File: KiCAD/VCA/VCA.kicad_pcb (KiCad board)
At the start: 4 copper layers, 30 x 100 mm, 17 parts, among them J1 VIN, J2 VC, J3 VOUT, J4 Conn_01x03_Pin, Q1 J172, Q2 J172, U1 LT1006

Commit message: Make VCA 2-Layer
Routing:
- net VSS: track 0.00 -> 62.0 mm
- net VDD: track 0.00 -> 2.69 mm
- net Net-(Q2-D): track 33.1 -> 31.8 mm
- added copper zone on B.Cu, net VDD
- removed copper zone on B.Cu, net GND
- removed copper zone on In1.Cu, net VDD
- removed copper zone on In2.Cu, net VSS
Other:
- copper layers 4 -> 2
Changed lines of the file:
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@@
 	(layers
 		(0 "F.Cu" signal)
-		(4 "In1.Cu" signal)
-		(6 "In2.Cu" signal)
 		(2 "B.Cu" signal)
 		(9 "F.Adhes" user "F.Adhesive")
@@
 			)
 			(layer "dielectric 1"
-				(type "prepreg")
-				(thickness 0.1)
-				(material "FR4")
-				(epsilon_r 4.5)
-				(loss_tangent 0.02)
-			)
-			(layer "In1.Cu"
-				(type "copper")
-				(thickness 0.035)
-			)
-			(layer "dielectric 2"
 				(type "core")
-				(thickness 1.24)
-				(material "FR4")
-				(epsilon_r 4.5)
-				(loss_tangent 0.02)
-			)
-			(layer "In2.Cu"
-				(type "copper")
-				(thickness 0.035)
-			)
-			(layer "dielectric 3"
-				(type "prepreg")
-				(thickness 0.1)
+				(thickness 1.51)
 				(material "FR4")
 				(epsilon_r 4.5)
@@
 			(net 0)
 			(net_name "")
-			(layers "F.Cu" "In1.Cu" "In2.Cu")
+			(layer "F.Cu")
 			(hatch full 0.508)
 			(connect_pads
@@
 			(net 0)
 			(net_name "")
-			(layers "F.Cu" "In1.Cu" "In2.Cu")
+			(layer "F.Cu")
 			(hatch full 0.508)
 			(connect_pads
@@
 			(net 0)
 			(net_name "")
-			(layers "F.Cu" "In1.Cu" "In2.Cu")
+			(layer "F.Cu")
 			(hatch full 0.508)
 			(connect_pads
@@
 	)
 	(segment
+		(start 124.5 100.115001)
+		(end 124.5 92.000001)
+		(width 0.5)
+		(layer "F.Cu")
+		(net 1)
+	)
+	(segment
+		(start 124.5 92.000001)
+		(end 127.5 89.000001)
+		(width 0.5)
+		(layer "F.Cu")
+		(net 1)
+	)
+	(segment
+		(start 126.195 101.810001)
+		(end 124.5 100.115001)
+		(width 0.5)
+		(layer "F.Cu")
+		(net 1)
+	)
+	(segment
+		(start 130 105.615001)
+		(end 130 111.385404)
+		(width 0.5)
+		(layer "B.Cu")
+		(net 1)
+	)
+	(segment
+		(start 139.5 120.885404)
+		(end 139.5 143.55)
+		(width 0.5)
+		(layer "B.Cu")
+		(net 1)
+	)
+	(segment
+		(start 130 111.385404)
+		(end 139.5 120.885404)
+		(width 0.5)
+		(layer "B.Cu")
+		(net 1)
+	)
+	(segment
+		(start 126.195 101.810001)
+		(end 130 105.615001)
+		(width 0.5)
+		(layer "B.Cu")
+		(net 1)
+	)
+	(segment
+		(start 137.5 136.6)
+		(end 139.4 134.7)
+		(width 0.5)
+		(layer "F.Cu")
+		(net 2)
+	)
+	(segment
 		(start 125.04 62.62)
 		(end 125.04 77.43)
@@
 		(end 136.999999 110.000001)
 		(width 0.2)
-		(layer "F.Cu")
-		(net 9)
-	)
-	(segment
-		(start 136.999999 110.000001)
-		(end 141.75 105.25)
-		(width 0.2)
-		(layer "F.Cu")
-		(net 9)
-	)
-	(segment
-		(start 141.75 105.25)
-		(end 141.75 101.87)
-		(width 0.2)
-		(layer "F.Cu")
+		(layer "B.Cu")
 		(net 9)
 	)
@@
 	)
 	(segment
-		(start 135.23 110.000001)
-		(end 135.23 108.48)
+		(start 127.597884 102.367885)
+		(end 127.597884 100.672885)
 		(width 0.2)
 		(layer "B.Cu")
@@
 	)
 	(segment
-		(start 122.5 100.25)
-		(end 123.48 99.27)
+		(start 136.999999 110.000001)
+		(end 141.25 105.75)
 		(width 0.2)
 		(layer "B.Cu")
@@
 	)
 	(segment
-		(start 130 101.25)
-		(end 130 103.25)
+		(start 127.597884 100.672885)
+		(end 126.195 99.270001)
 		(width 0.2)
 		(layer "B.Cu")
@@
 	)
 	(segment
-		(start 135.23 108.48)
-		(end 130 103.25)
+		(start 135.23 110.000001)
+		(end 127.597884 102.367885)
 		(width 0.2)
 		(layer "B.Cu")
@@
 	)
 	(segment
-		(start 128.02 99.27)
-		(end 130 101.25)
+		(start 122.5 100.25)
+		(end 123.48 99.27)
 		(width 0.2)
 		(layer "B.Cu")
@@
 	)
 	(segment
-		(start 126.195 99.27)
-		(end 128.02 99.27)
+		(start 123.48 99.27)
+		(end 126.195 99.27)
 		(width 0.2)
 		(layer "B.Cu")
@@
 	)
 	(segment
-		(start 123.48 99.27)
-		(end 126.195 99.27)
+		(start 141.25 105.75)
+		(end 141.25 101.87)
 		(width 0.2)
 		(layer "B.Cu")
@@
 	)
 	(zone
-		(net 4)
-		(net_name "GND")
+		(net 2)
+		(net_name "VDD")
 		(layer "B.Cu")
 		(hatch edge 0.5)
@@
 			)
 		)
-	)
-	(zone
-		(net 2)
-		(net_name "VDD")
-		(layer "In1.Cu")
-		(hatch edge 0.5)
-		(priority 1)
-		(connect_pads
-			(clearance 0.5)
-		)
-		(min_thickness 0.25)
-		(filled_areas_thickness no)
-		(fill yes
-			(thermal_gap 0.5)
-			(thermal_bridge_width 0.5)
-		)
-		(polygon
-			(pts
-				(xy 109.75 44.75) (xy 149.75 44.75) (xy 149.75 154.75) (xy 109.75 154.75)
-			)
-		)
-	)
-	(zone
-		(net 1)
-		(net_name "VSS")
-		(layer "In2.Cu")
-		(hatch edge 0.5)
-		(priority 2)
-		(connect_pads
-			(clearance 0.5)
-		)
-		(min_thickness 0.25)
-		(filled_areas_thickness no)
-		(fill yes
-			(thermal_gap 0.5)
-			(thermal_bridge_width 0.5)
-		)
-		(polygon
-			(pts
-				(xy 110.75 45.75) (xy 150.75 45.75) (xy 150.75 155.75) (xy 110.75 155.75)
-			)
-		)

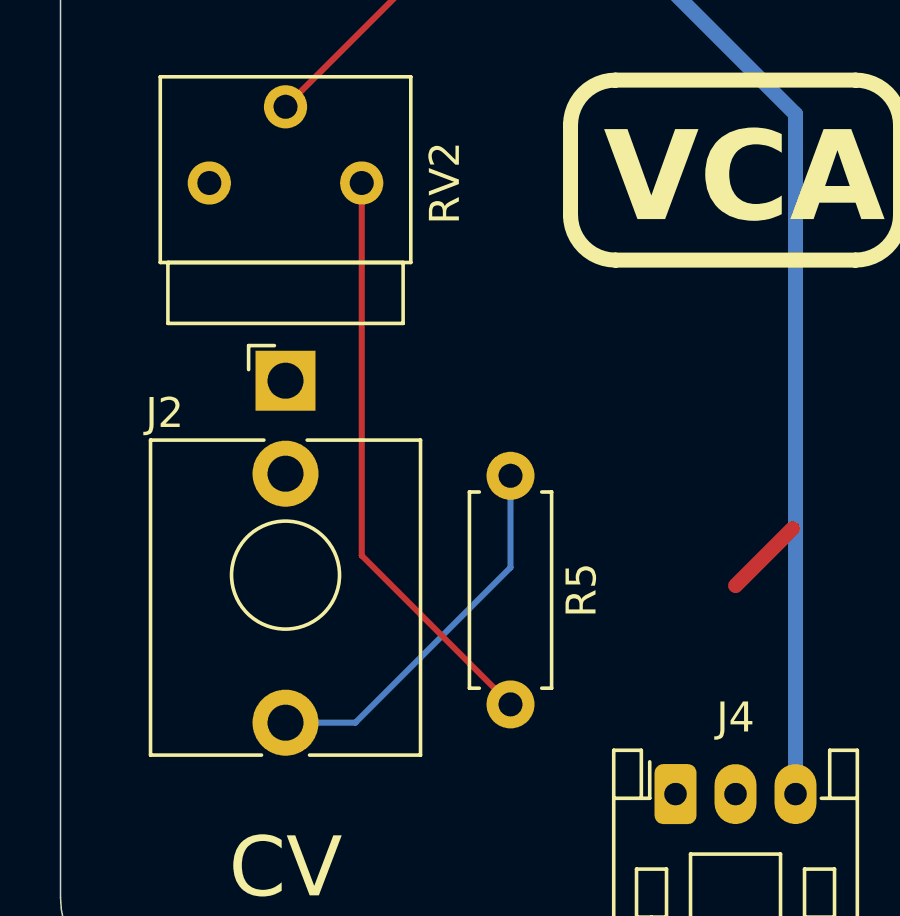
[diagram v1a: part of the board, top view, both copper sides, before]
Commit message: VCA - Minor Trace Edit
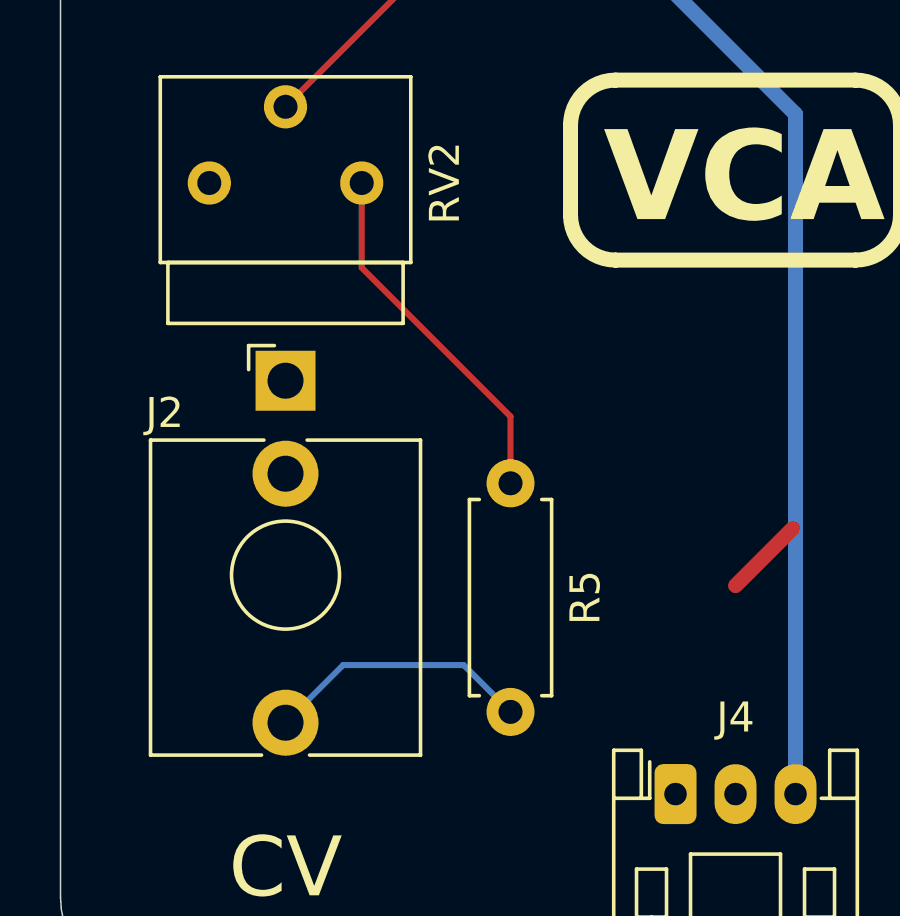
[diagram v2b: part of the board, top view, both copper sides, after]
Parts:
- moved R5 7.87 mm to (130.0, 140.8), turned to 90 degrees
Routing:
- net Net-(R5-Pad2): track 19.4 -> 12.3 mm
- net Net-(J2-PadT): track 12.9 -> 9.45 mm

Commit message: Mixer PCB - Gerbers
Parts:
- added REF**: Untitled, HackSynth:Module 30x100mm, F.Cu at (130.0, 100.0)
- moved J4 0.50 mm to (136.0, 143.6)
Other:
- board text added: "VCA v1-1 - PancakeLegend 2025"
- board text removed: "VCA v1-0 - PancakeLegend 2025"
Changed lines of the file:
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@@
 	)
 	(paper "A4")
+	(title_block
+		(title "VCA")
+		(date "2025-06-14")
+		(rev "1-1")
+	)
 	(layers
 		(0 "F.Cu" signal)
@@
 	(footprint "HackSynth:JST_PH_S3B-PH-K_1x03_P2.00mm_Horizontal"
 		(layer "F.Cu")
-		(at 135.5 143.55)
+		(at 136 143.55)
 		(descr "JST PH series connector, S3B-PH-K (http://www.jst-mfg.com/product/pdf/eng/ePH.pdf), generated with kicad-footprint-generator")
 		(tags "connector JST PH horizontal")
@@
 		)
 	)
+	(footprint "HackSynth:Module 30x100mm"
+		(layer "F.Cu")
+		(at 130 100)
+		(property "Reference" "REF**"
+			(at 0 -0.5 0)
+			(unlocked yes)
+			(layer "F.SilkS")
+			(hide yes)
+			(effects
+				(font
+					(size 1 1)
+					(thickness 0.1)
+				)
+			)
+		)
+		(property "Value" "Untitled"
+			(at 0 1 0)
+			(unlocked yes)
+			(layer "F.Fab")
+			(hide yes)
+			(effects
+				(font
+					(size 1 1)
+					(thickness 0.15)
+				)
+			)
+		)
+		(property "Datasheet" ""
+			(at 0 0 0)
+			(unlocked yes)
+			(layer "F.Fab")
+			(hide yes)
+			(effects
+				(font
+					(size 1 1)
+					(thickness 0.15)
+				)
+			)
+		)
+		(property "Description" ""
+			(at 0 0 0)
+			(unlocked yes)
+			(layer "F.Fab")
+			(hide yes)
+			(effects
+				(font
+					(size 1 1)
+					(thickness 0.15)
+				)
+			)
+		)
+		(attr smd)
+		(fp_line
+			(start -9 46)
+			(end -7 46)
+			(stroke
+				(width 0.1)
+				(type default)
+			)
+			(layer "Dwgs.User")
+		)
+		(fp_line
+			(start -8 45)
+			(end -8 47)
+			(stroke
+				(width 0.1)
+				(type default)
+			)
+			(layer "Dwgs.User")
+		)
+		(fp_line
+			(start 7 46)
+			(end 9 46)
+			(stroke
+				(width 0.1)
+				(type default)
+			)
+			(layer "Dwgs.User")
+		)
+		(fp_line
+			(start 8 45)
+			(end 8 47)
+			(stroke
+				(width 0.1)
+				(type default)
+			)
+			(layer "Dwgs.User")
+		)
+		(fp_line
+			(start -14.999999 -47)
+			(end -15 47)
+			(stroke
+				(width 0.05)
+				(type default)
+			)
+			(layer "Edge.Cuts")
+		)
+		(fp_line
+			(start -12 49.999999)
+			(end 12 50)
+			(stroke
+				(width 0.05)
+				(type default)
+			)
+			(layer "Edge.Cuts")
+		)
+		(fp_line
+			(start 12 -50)
+			(end -12 -50)
+			(stroke
+				(width 0.05)
+				(type default)
+			)
+			(layer "Edge.Cuts")
+		)
+		(fp_line
+			(start 15 47)
+			(end 15 -47)
+			(stroke
+				(width 0.05)
+				(type default)
+			)
+			(layer "Edge.Cuts")
+		)
+		(fp_arc
+			(start -15 -47)
+			(mid -14.12132 -49.12132)
+			(end -12 -50)
+			(stroke
+				(width 0.05)
+				(type default)
+			)
+			(layer "Edge.Cuts")
+		)
+		(fp_arc
+			(start -12 50)
+			(mid -14.12132 49.12132)
+			(end -15 47)
+			(stroke
+				(width 0.05)
+				(type default)
+			)
+			(layer "Edge.Cuts")
+		)
+		(fp_arc
+			(start 12 -50)
+			(mid 14.12132 -49.12132)
+			(end 15 -47)
+			(stroke
+				(width 0.05)
+				(type default)
+			)
+			(layer "Edge.Cuts")
+		)
+		(fp_arc
+			(start 15 47)
+			(mid 14.12132 49.12132)
+			(end 12 50)
+			(stroke
+				(width 0.05)
+				(type default)
+			)
+			(layer "Edge.Cuts")
+		)
+		(embedded_fonts no)
+	)
 	(footprint "HackSynth:Jack_3.5mm"
 		(layer "F.Cu")
@@
 		(layer "F.SilkS")
 	)
-	(gr_arc
-		(start 144.999999 147)
-		(mid 144.121319 149.12132)
-		(end 141.999999 150)
-		(stroke
-			(width 0.05)
-			(type default)
-		)
-		(layer "Edge.Cuts")
-	)
-	(gr_line
-		(start 142 50)
-		(end 118 50)
-		(stroke
-			(width 0.05)
-			(type default)
-		)
-		(layer "Edge.Cuts")
-	)
-	(gr_arc
-		(start 114.999999 52.999999)
-		(mid 115.878679 50.878679)
-		(end 117.999999 49.999999)
-		(stroke
-			(width 0.05)
-			(type default)
-		)
-		(layer "Edge.Cuts")
-	)
-	(gr_line
-		(start 115 146.999999)
-		(end 115 52.999999)
-		(stroke
-			(width 0.05)
-			(type default)
-		)
-		(layer "Edge.Cuts")
-	)
-	(gr_arc
-		(start 118 149.999999)
-		(mid 115.87868 149.121319)
-		(end 115 146.999999)
-		(stroke
-			(width 0.05)
-			(type default)
-		)
-		(layer "Edge.Cuts")
-	)
-	(gr_line
-		(start 142 150)
-		(end 118 150)
-		(stroke
-			(width 0.05)
-			(type default)
-		)
-		(layer "Edge.Cuts")
-	)
-	(gr_arc
-		(start 142 50)
-		(mid 144.12132 50.87868)
-		(end 145 53)
-		(stroke
-			(width 0.05)
-			(type default)
-		)
-		(layer "Edge.Cuts")
-	)
-	(gr_line
-		(start 145 53)
-		(end 144.999999 147)
-		(stroke
-			(width 0.05)
-			(type default)
-		)
-		(layer "Edge.Cuts")
-	)
 	(gr_text "IN"
 		(at 122.5 55 0)
@@
 		)
 	)
-	(gr_text "VCA v1-0 - PancakeLegend 2025"
+	(gr_text "VCA v1-1 - PancakeLegend 2025"
 		(at 141.75 88.25 270)
 		(layer "B.SilkS")
@@
 	(segment
 		(start 130 105.615001)
-		(end 130 111.385404)
+		(end 126.195 101.810001)
 		(width 0.5)
 		(layer "B.Cu")
@@
 	)
 	(segment
-		(start 139.5 120.885404)
-		(end 139.5 143.55)
+		(start 130 111.385404)
+		(end 130 105.615001)
 		(width 0.5)
 		(layer "B.Cu")
@@
 	)
 	(segment
-		(start 130 111.385404)
-		(end 139.5 120.885404)
+		(start 140 121.385404)
+		(end 130 111.385404)
 		(width 0.5)
 		(layer "B.Cu")
@@
 	)
 	(segment
-		(start 126.195 101.810001)
-		(end 130 105.615001)
+		(start 140 143.55)
+		(end 140 121.385404)
 		(width 0.5)
 		(layer "B.Cu")

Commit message: Review
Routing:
- net VDD: track 2.69 -> 0.00 mm
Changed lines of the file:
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@@
 		)
 		(embedded_fonts no)
-		(model "${KICAD9_3DMODEL_DIR}/Package_DIP.3dshapes/DIP-8_W7.62mm.wrl"
+		(model "${KICAD9_3DMODEL_DIR}/Package_DIP.3dshapes/DIP-8_W7.62mm.step"
 			(offset
 				(xyz 0 0 0)
@@
 			(layer "F.SilkS")
 		)
-		(fp_line
-			(start 6.05 1.5)
-			(end 6.05 -1.5)
-			(stroke
-				(width 0.05)
-				(type solid)
-			)
-			(layer "F.CrtYd")
-		)
-		(fp_line
-			(start 6.05 -1.5)
-			(end -1.05 -1.5)
-			(stroke
-				(width 0.05)
-				(type solid)
-			)
-			(layer "F.CrtYd")
-		)
-		(fp_line
-			(start -1.05 1.5)
-			(end 6.05 1.5)
-			(stroke
-				(width 0.05)
-				(type solid)
-			)
-			(layer "F.CrtYd")
-		)
-		(fp_line
+		(fp_rect
 			(start -1.05 -1.5)
-			(end -1.05 1.5)
+			(end 6.05 1.5)
 			(stroke
 				(width 0.05)
 				(type solid)
 			)
+			(fill no)
 			(layer "F.CrtYd")
 		)
-		(fp_line
-			(start 5 1.25)
-			(end 5 -1.25)
-			(stroke
-				(width 0.1)
-				(type solid)
-			)
-			(layer "F.Fab")
-		)
-		(fp_line
-			(start 5 -1.25)
-			(end 0 -1.25)
-			(stroke
-				(width 0.1)
-				(type solid)
-			)
-			(layer "F.Fab")
-		)
-		(fp_line
-			(start 0 1.25)
-			(end 5 1.25)
-			(stroke
-				(width 0.1)
-				(type solid)
-			)
-			(layer "F.Fab")
-		)
-		(fp_line
+		(fp_rect
 			(start 0 -1.25)
-			(end 0 1.25)
+			(end 5 1.25)
 			(stroke
 				(width 0.1)
 				(type solid)
 			)
+			(fill no)
 			(layer "F.Fab")
 		)
@@
 		)
 		(embedded_fonts no)
-		(model "${KICAD9_3DMODEL_DIR}/Capacitor_THT.3dshapes/C_Disc_D5.0mm_W2.5mm_P5.00mm.wrl"
+		(model "${KICAD9_3DMODEL_DIR}/Capacitor_THT.3dshapes/C_Disc_D5.0mm_W2.5mm_P5.00mm.step"
 			(offset
 				(xyz 0 0 0)
@@
 		(fp_line
 			(start 0 0)
-			(end 0.659999 0)
+			(end 0.66 0)
 			(stroke
 				(width 0.1)
@@
 	)
 	(segment
-		(start 137.5 136.6)
-		(end 139.4 134.7)
-		(width 0.5)
-		(layer "F.Cu")
-		(net 2)
-	)
-	(segment
